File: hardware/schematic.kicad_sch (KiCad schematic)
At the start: 2 parts

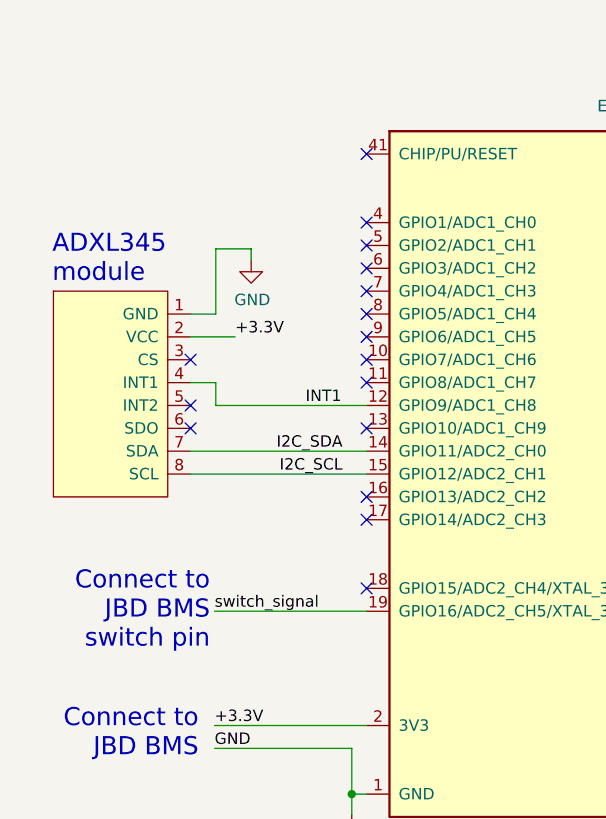
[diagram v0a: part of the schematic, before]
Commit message: Updated the schematic based on latest firmware. Firmware detects correclty the movement and deep sleeps
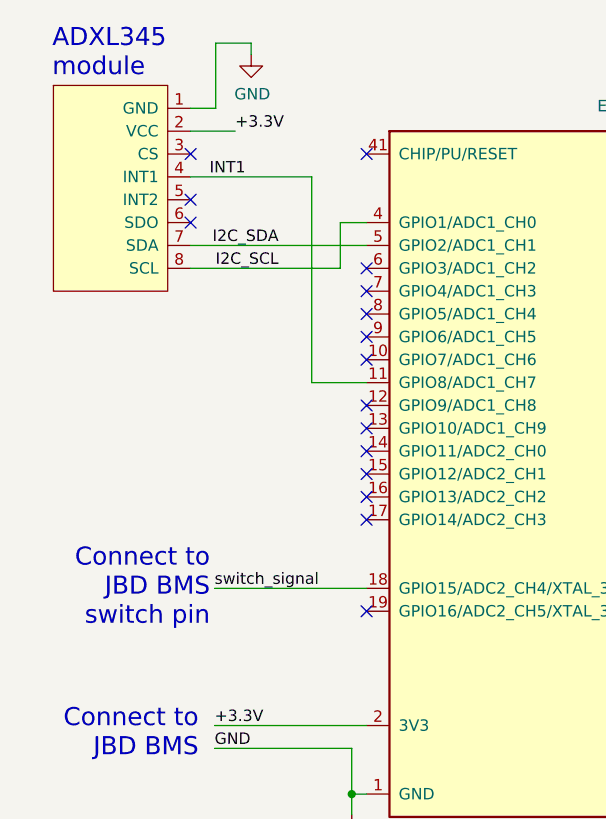
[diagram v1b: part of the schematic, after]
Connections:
- net I2C_SCL: now also U?.4 (GPIO1/ADC1_CH0); no longer U?.15 (GPIO12/ADC2_CH1)
- net I2C_SDA: now also U?.5 (GPIO2/ADC1_CH1); no longer U?.14 (GPIO11/ADC2_CH0)
- net INT1: now also U?.11 (GPIO8/ADC1_CH7); no longer U?.12 (GPIO9/ADC1_CH8)
- net switch_signal: now also U?.18 (GPIO15/ADC2_CH4/XTAL_32K_P); no longer U?.19 (GPIO16/ADC2_CH5/XTAL_32K_N)
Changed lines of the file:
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@@
   )
   (no_connect (at 248.539 173.863))
-  (no_connect (at 157.861 135.763))
-  (no_connect (at 157.861 128.143))
+  (no_connect (at 177.419 156.083))
+  (no_connect (at 157.861 112.903))
+  (no_connect (at 157.861 105.283))
   (no_connect (at 248.539 176.403))
-  (no_connect (at 177.419 153.543))
+  (no_connect (at 177.419 133.223))
+  (no_connect (at 177.419 140.843))
   (no_connect (at 177.419 145.923))
   (no_connect (at 248.539 153.416))
@@
   (no_connect (at 248.539 171.323))
   (no_connect (at 177.419 143.383))
-  (no_connect (at 177.419 130.683))
   (no_connect (at 177.419 125.603))
   (no_connect (at 177.419 105.283))
   (no_connect (at 177.419 123.063))
   (no_connect (at 177.419 135.763))
-  (no_connect (at 177.419 112.903))
   (no_connect (at 177.419 120.523))
   (no_connect (at 177.419 117.983))
-  (no_connect (at 177.419 115.443))
   (no_connect (at 248.539 107.823))
   (no_connect (at 248.539 120.523))
@@
   (no_connect (at 248.539 130.683))
   (no_connect (at 248.539 140.843))
+  (no_connect (at 177.419 138.303))
   (no_connect (at 177.419 128.143))
   (no_connect (at 248.539 123.063))
-  (no_connect (at 157.861 133.223))
+  (no_connect (at 157.861 110.363))
   (no_connect (at 248.539 117.983))
-  (wire (pts (xy 164.592 115.824) (xy 164.592 117.094))
+  (wire (pts (xy 164.592 92.964) (xy 164.592 94.234))
     (stroke (width 0) (type default) (color 0 0 0 1))
   )
@@
     (stroke (width 0) (type default) (color 0 0 0 1))
   )
-  (wire (pts (xy 157.861 123.063) (xy 160.655 123.063))
+  (wire (pts (xy 177.419 130.683) (xy 171.323 130.683))
+    (stroke (width 0) (type default))
+  )
+  (wire (pts (xy 157.861 100.203) (xy 160.655 100.203))
     (stroke (width 0) (type default) (color 0 0 0 1))
   )
@@
     (stroke (width 0) (type default) (color 0 0 0 1))
   )
-  (wire (pts (xy 160.655 133.223) (xy 160.655 130.683))
-    (stroke (width 0) (type default))
-  )
   (wire (pts (xy 175.768 176.403) (xy 177.419 176.403))
     (stroke (width 0) (type default) (color 0 0 0 1))
   )
-  (wire (pts (xy 160.655 123.063) (xy 160.655 115.824))
-    (stroke (width 0) (type default) (color 0 0 0 1))
-  )
-  (wire (pts (xy 157.861 130.683) (xy 160.655 130.683))
-    (stroke (width 0) (type default))
-  )
-  (wire (pts (xy 157.861 138.303) (xy 177.419 138.303))
-    (stroke (width 0) (type default))
-  )
-  (wire (pts (xy 160.655 115.824) (xy 164.592 115.824))
-    (stroke (width 0) (type default) (color 0 0 0 1))
-  )
-  (wire (pts (xy 157.861 140.843) (xy 177.419 140.843))
+  (wire (pts (xy 160.655 100.203) (xy 160.655 92.964))
+    (stroke (width 0) (type default) (color 0 0 0 1))
+  )
+  (wire (pts (xy 171.323 130.683) (xy 171.323 107.823))
+    (stroke (width 0) (type default))
+  )
+  (wire (pts (xy 157.861 107.823) (xy 171.323 107.823))
+    (stroke (width 0) (type default))
+  )
+  (wire (pts (xy 160.655 92.964) (xy 164.592 92.964))
+    (stroke (width 0) (type default) (color 0 0 0 1))
+  )
+  (wire (pts (xy 157.861 117.983) (xy 174.498 117.983))
+    (stroke (width 0) (type default))
+  )
+  (wire (pts (xy 160.528 153.543) (xy 177.419 153.543))
     (stroke (width 0) (type default))
   )
@@
     (stroke (width 0) (type default) (color 0 0 0 1))
   )
-  (wire (pts (xy 157.861 125.603) (xy 162.814 125.603))
+  (wire (pts (xy 157.861 102.743) (xy 162.814 102.743))
     (stroke (width 0) (type default) (color 194 0 0 1))
   )
-  (wire (pts (xy 160.528 156.083) (xy 177.419 156.083))
+  (wire (pts (xy 157.861 115.443) (xy 177.419 115.443))
     (stroke (width 0) (type default))
   )
@@
     (stroke (width 0) (type default) (color 194 0 0 1))
   )
-  (wire (pts (xy 177.419 133.223) (xy 160.655 133.223))
-    (stroke (width 0) (type default))
-  )
-  (text "Connect to\nJBD BMS\nswitch pin" (at 160.02 160.401 0)
-    (effects (font (size 2.0066 2.0066)) (justify right bottom))
-  )
-  (text "ADXL345\nmodule" (at 142.494 119.761 0)
+  (wire (pts (xy 177.419 112.903) (xy 174.498 112.903))
+    (stroke (width 0) (type default))
+  )
+  (wire (pts (xy 174.498 112.903) (xy 174.498 117.983))
+    (stroke (width 0) (type default))
+  )
+  (text "ADXL345\nmodule" (at 142.494 96.901 0)
     (effects (font (size 2.0066 2.0066)) (justify left bottom))
   )
@@
     (effects (font (size 2.0066 2.0066)) (justify right bottom))
   )
+  (text "Connect to\nJBD BMS\nswitch pin" (at 160.02 157.861 0)
+    (effects (font (size 2.0066 2.0066)) (justify right bottom))
+  )
+  (label "INT1" (at 163.957 107.823 180) (fields_autoplaced)
+    (effects (font (size 1.27 1.27)) (justify right bottom))
+  )
+  (label "I2C_SDA" (at 167.64 115.443 180) (fields_autoplaced)
+    (effects (font (size 1.27 1.27)) (justify right bottom))
+  )
   (label "GND" (at 160.528 171.323 0) (fields_autoplaced)
     (effects (font (size 1.27 1.27)) (justify left bottom))
@@
     (effects (font (size 1.27 1.27)) (justify left bottom))
   )
-  (label "switch_signal" (at 160.528 156.083 0) (fields_autoplaced)
-    (effects (font (size 1.27 1.27)) (justify left bottom))
-  )
-  (label "INT1" (at 174.625 133.223 180) (fields_autoplaced)
+  (label "+3.3V" (at 162.814 102.743 0) (fields_autoplaced)
+    (effects (font (size 1.27 1.27)) (justify left bottom))
+  )
+  (label "switch_signal" (at 160.528 153.543 0) (fields_autoplaced)
+    (effects (font (size 1.27 1.27)) (justify left bottom))
+  )
+  (label "I2C_SCL" (at 167.64 117.983 180) (fields_autoplaced)
     (effects (font (size 1.27 1.27)) (justify right bottom))
   )
-  (label "+3.3V" (at 162.814 125.603 0) (fields_autoplaced)
-    (effects (font (size 1.27 1.27)) (justify left bottom))
-  )
-  (label "I2C_SDA" (at 174.752 138.303 180) (fields_autoplaced)
-    (effects (font (size 1.27 1.27)) (justify right bottom))
-  )
-  (label "I2C_SCL" (at 174.752 140.843 180) (fields_autoplaced)
-    (effects (font (size 1.27 1.27)) (justify right bottom))
-  )
-  (symbol (lib_id "schematic-OLED_SPI-Bafang_M500_M600-rescue:SSD1306-SPI-OLED-schematic-rescue") (at 148.971 131.953 0) (unit 1)
+  (symbol (lib_id "schematic-OLED_SPI-Bafang_M500_M600-rescue:SSD1306-SPI-OLED-schematic-rescue") (at 148.971 109.093 0) (unit 1)
     (in_bom yes) (on_board yes) (dnp no)
-    (property "Reference" "NA?" (at 147.7264 122.9868 0)
+    (property "Reference" "NA?" (at 147.7264 100.1268 0)
       (effects (font (size 1.27 1.27)) (justify right) hide)
     )
-    (property "Value" "ADXL345\nmodule" (at 152.781 117.983 0)
+    (property "Value" "ADXL345\nmodule" (at 152.781 95.123 0)
       (effects (font (size 1.27 1.27)) (justify right) hide)
     )
-    (property "Footprint" "" (at 152.781 137.033 90)
-      (effects (font (size 1.27 1.27)) hide)
-    )
-    (property "Datasheet" "" (at 152.781 137.033 90)
+    (property "Footprint" "" (at 152.781 114.173 90)
+      (effects (font (size 1.27 1.27)) hide)
+    )
+    (property "Datasheet" "" (at 152.781 114.173 90)
       (effects (font (size 1.27 1.27)) hide)
     )
@@
     )
   )
-  (symbol (lib_id "power:GND") (at 164.592 117.094 0) (unit 1)
+  (symbol (lib_id "power:GND") (at 164.592 94.234 0) (unit 1)
     (in_bom yes) (on_board yes) (dnp no)
-    (property "Reference" "#PWR?" (at 164.592 123.444 0)
-      (effects (font (size 1.27 1.27)) hide)
-    )
-    (property "Value" "GND" (at 164.719 121.4882 0)
+    (property "Reference" "#PWR?" (at 164.592 100.584 0)
+      (effects (font (size 1.27 1.27)) hide)
+    )
+    (property "Value" "GND" (at 164.719 98.6282 0)
       (effects (font (size 1.27 1.27)))
     )
-    (property "Footprint" "" (at 164.592 117.094 0)
-      (effects (font (size 1.27 1.27)) hide)
-    )
-    (property "Datasheet" "" (at 164.592 117.094 0)
-      (effects (font (size 1.27 1.27)) hide)
-    )
+    (property "Footprint" "" (at 164.592 94.234 0)
+      (effects (font (size 1.27 1.27)) hide)
+    )
+    (property "Datasheet" "" (at 164.592 94.234 0)
+      (effects (font (size 1.27 1.27)) hide)
+    )

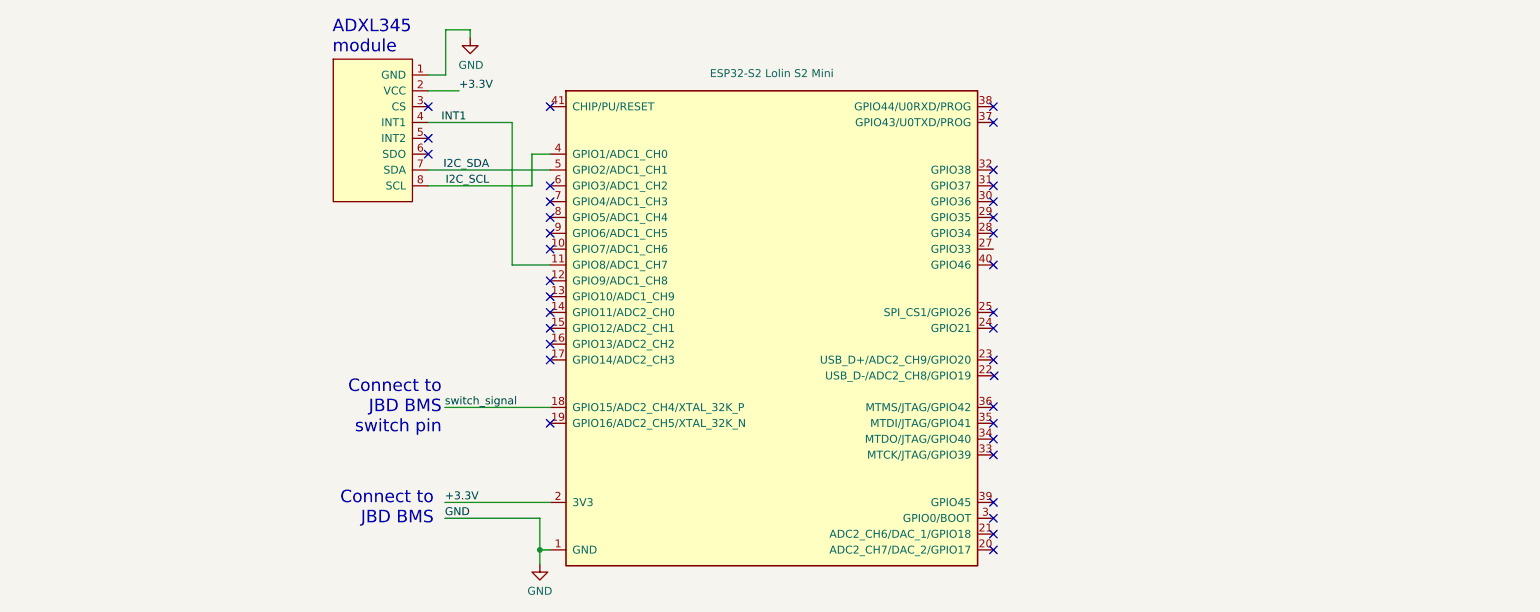
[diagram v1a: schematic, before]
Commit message: Corrected switch pin schematic and firmware. Added pictures of the built unit
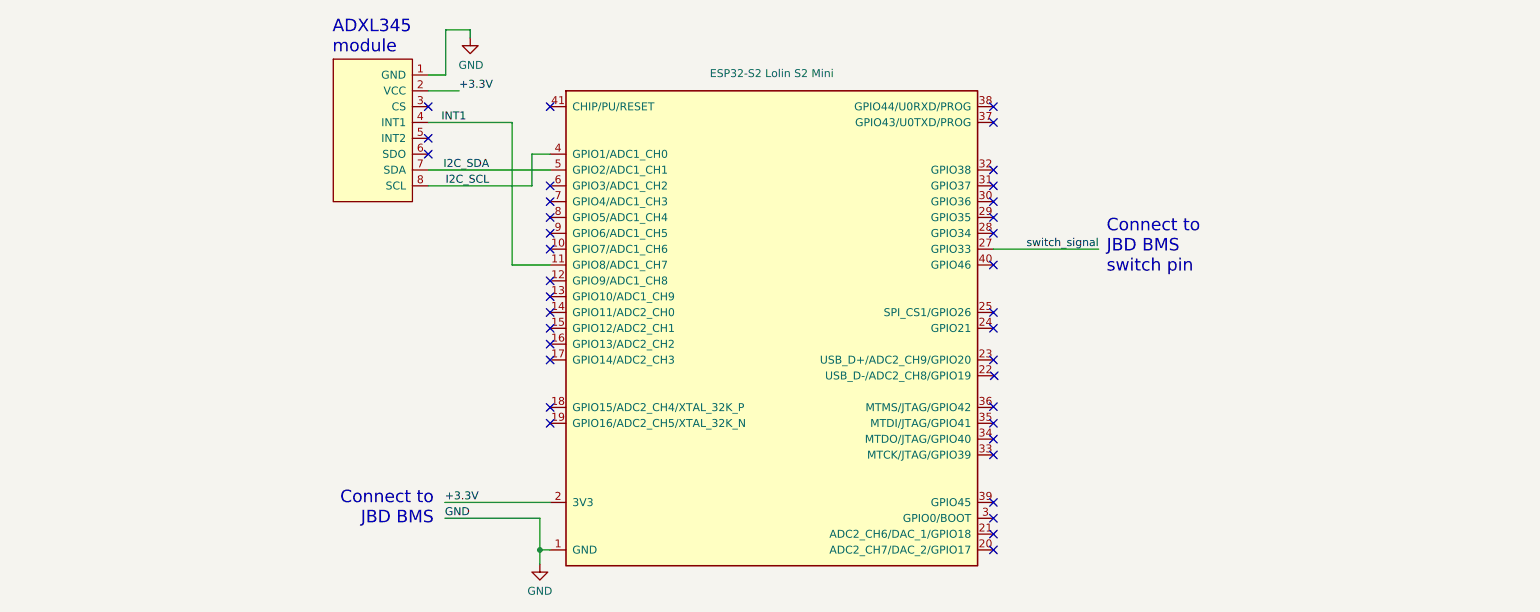
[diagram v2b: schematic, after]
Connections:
- net switch_signal: now also U?.27 (GPIO33); no longer U?.18 (GPIO15/ADC2_CH4/XTAL_32K_P)
- no-connect marks 36 -> 37
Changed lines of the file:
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@@
   (no_connect (at 157.861 112.903))
   (no_connect (at 157.861 105.283))
+  (no_connect (at 177.419 153.543))
   (no_connect (at 248.539 176.403))
   (no_connect (at 177.419 133.223))
@@
   (no_connect (at 157.861 110.363))
   (no_connect (at 248.539 117.983))
+  (wire (pts (xy 265.43 128.143) (xy 248.539 128.143))
+    (stroke (width 0) (type default))
+  )
   (wire (pts (xy 164.592 92.964) (xy 164.592 94.234))
     (stroke (width 0) (type default) (color 0 0 0 1))
@@
     (stroke (width 0) (type default))
   )
-  (wire (pts (xy 160.528 153.543) (xy 177.419 153.543))
-    (stroke (width 0) (type default))
-  )
   (wire (pts (xy 175.768 176.403) (xy 175.768 178.689))
     (stroke (width 0) (type default) (color 0 0 0 1))
@@
     (stroke (width 0) (type default))
   )
+  (text "Connect to\nJBD BMS\nswitch pin" (at 266.7 132.08 0)
+    (effects (font (size 2.0066 2.0066)) (justify left bottom))
+  )
   (text "ADXL345\nmodule" (at 142.494 96.901 0)
     (effects (font (size 2.0066 2.0066)) (justify left bottom))
   )
   (text "Connect to\nJBD BMS" (at 158.75 172.466 0)
-    (effects (font (size 2.0066 2.0066)) (justify right bottom))
-  )
-  (text "Connect to\nJBD BMS\nswitch pin" (at 160.02 157.861 0)
     (effects (font (size 2.0066 2.0066)) (justify right bottom))
   )
@@
     (effects (font (size 1.27 1.27)) (justify left bottom))
   )
+  (label "switch_signal" (at 265.43 128.143 180) (fields_autoplaced)
+    (effects (font (size 1.27 1.27)) (justify right bottom))
+  )
   (label "+3.3V" (at 162.814 102.743 0) (fields_autoplaced)
     (effects (font (size 1.27 1.27)) (justify left bottom))
   )
-  (label "switch_signal" (at 160.528 153.543 0) (fields_autoplaced)
-    (effects (font (size 1.27 1.27)) (justify left bottom))
-  )

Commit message: Updated the shcematic and documentation based on latest board I built
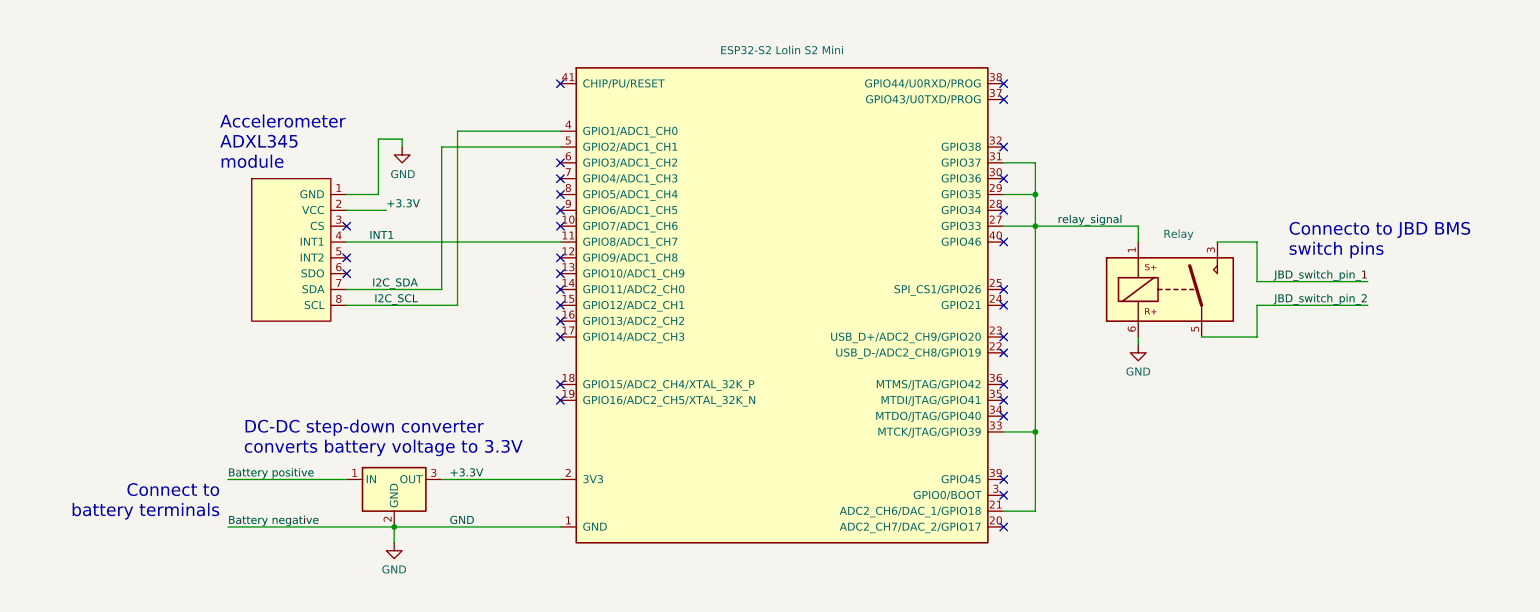
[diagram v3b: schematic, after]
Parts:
- added K1: Relay, Relay_THT:Relay_1P1T_NO_10x24x18.8mm_Panasonic_ADW11xxxxW_THT, symbol Relay:ADW11
- added U1: Step-down converter to 3.3V, Converter_DCDC:Converter_DCDC_Murata_OKI-78SR_Vertical, symbol Converter_DCDC:OKI-78SR-3.3_1.5-W36-C
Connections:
- net switch_signal is gone; now on net relay_signal: U?.27 (GPIO33)
- net +3.3V: now also U1.3 (OUT)
- net GND: now also K1.6, U1.2 (GND)
- net relay_signal: now reaches U?.21 (ADC2_CH6/DAC_1/GPIO18)
- net relay_signal: now also U?.29 (GPIO35), U?.31 (GPIO37), U?.33 (MTCK/JTAG/GPIO39), K1.1
- new net Battery positive: U1.1 (IN)
- new net JBD_switch_pin_1: K1.3
- new net JBD_switch_pin_2: K1.5
- no-connect marks 37 -> 33
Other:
- note added: "Accelerometer ADXL345 module"
- note added: "Connect to battery terminals"
- note added: "Connecto to JBD BMS switch pins"
- note added: "DC-DC step-down converter converts battery voltage to 3.3V"
- note removed: "ADXL345 module"
- note removed: "Connect to JBD BMS"
- note removed: "Connect to JBD BMS switch pin"
